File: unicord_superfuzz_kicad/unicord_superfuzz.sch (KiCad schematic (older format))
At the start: 60 parts

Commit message: Add values for most circuit elements
Have not yet added anything for transistors, switch, power supply.
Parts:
- C? (x12): value C -> 10uF
- C?: value C -> 0.002
- C? (x2): value C -> 0.1uF
- C?: value C -> 0.001uF
- R? (x7): value R_US -> 10k
- R? (x3): value R_US -> 470k
- R? (x2): value R_US -> 1.8k
- R? (x3): value R_US -> 47k
- R? (x6): value R_US -> 100k
- R? (x4): value R_US -> 22k
- R?: value R_US -> 150k
- R?: value R_US -> 220k
- R?: value R_US -> 3.3k
- R?: value R_US -> 15k
- R?: value R_US -> 1k
- RV?: value R_POT_US -> 10k
- RV? (x2): value R_POT_US -> 50k
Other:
- moved on the sheet: C?, D?, J?, Q?, R?, RV?, SW?

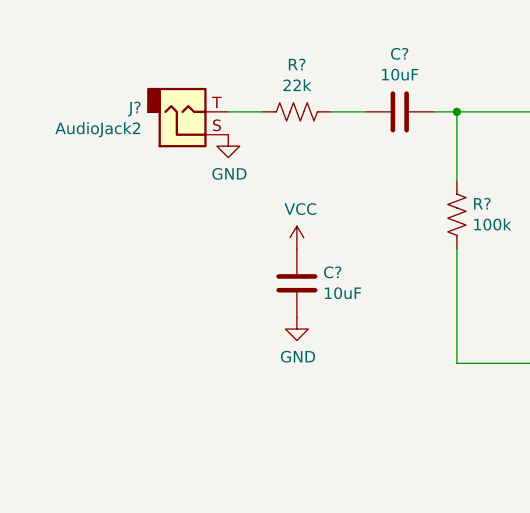
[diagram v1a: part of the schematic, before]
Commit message: Add power/ground to circuit
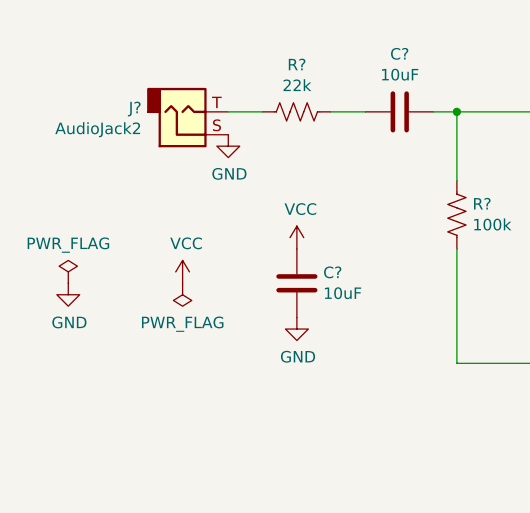
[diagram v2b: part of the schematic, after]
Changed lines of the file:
@@
 	0    1    1    0
 $EndComp
+$Comp
+L power:PWR_FLAG #FLG?
+U 1 1 5ECEB2A7
+P 5000 5950
+F 0 "#FLG?" H 5000 6025 50  0001 C CNN
+F 1 "PWR_FLAG" H 5000 6123 50  0000 C CNN
+F 2 "" H 5000 5950 50  0001 C CNN
+F 3 "~" H 5000 5950 50  0001 C CNN
+	1    5000 5950
+	1    0    0    1
+$EndComp
+$Comp
+L power:VCC #PWR?
+U 1 1 5ED00095
+P 5000 5950
+F 0 "#PWR?" H 5000 5800 50  0001 C CNN
+F 1 "VCC" H 5017 6123 50  0000 C CNN
+F 2 "" H 5000 5950 50  0001 C CNN
+F 3 "" H 5000 5950 50  0001 C CNN
+	1    5000 5950
+	1    0    0    -1
+$EndComp
+$Comp
+L power:PWR_FLAG #FLG?
+U 1 1 5ED3CD5C
+P 4500 5950
+F 0 "#FLG?" H 4500 6025 50  0001 C CNN
+F 1 "PWR_FLAG" H 4500 6123 50  0000 C CNN
+F 2 "" H 4500 5950 50  0001 C CNN
+F 3 "~" H 4500 5950 50  0001 C CNN
+	1    4500 5950
+	1    0    0    -1
+$EndComp
+$Comp
+L power:GND #PWR?
+U 1 1 5ED44778
+P 4500 5950
+F 0 "#PWR?" H 4500 5700 50  0001 C CNN
+F 1 "GND" H 4505 5777 50  0000 C CNN
+F 2 "" H 4500 5950 50  0001 C CNN
+F 3 "" H 4500 5950 50  0001 C CNN
+	1    4500 5950
+	1    0    0    -1
+$EndComp
 $EndSCHEMATC

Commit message: Add annotations to circuit elements
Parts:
- D1, D2: renamed from D?; value D -> DA-90
- gave numbers to parts that had none: 58

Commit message: Add footprints and .net file
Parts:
- C1, C10, C11, C12, C15, C16, C2, C5, C6, C7, C8, C9: footprint (none) -> Capacitor_THT:C_Radial_D5.0mm_H11.0mm_P2.00mm
- C13, C14, C3, C4: footprint (none) -> Capacitor_THT:C_Disc_D5.0mm_W2.5mm_P5.00mm
- D1, D2: footprint (none) -> Diode_THT:D_A-405_P12.70mm_Horizontal
- J1, J2: footprint (none) -> Connector_PinHeader_2.54mm:PinHeader_1x02_P2.54mm_Vertical
- Q1, Q2, Q3, Q4, Q5, Q6: footprint (none) -> Package_TO_SOT_THT:TO-92
- R1, R10, R11, R12, R13, R14, R15, R16, R17, R18, R19, R2, R20, R21, R22, R23, R24, R25, R26, R27, R28, R29, R3, R30, R4, R5, R6, R7, R8, R9: footprint (none) -> Resistor_THT:R_Axial_DIN0204_L3.6mm_D1.6mm_P7.62mm_Horizontal
- RV1, RV3, SW1: footprint (none) -> Connector_PinHeader_2.54mm:PinHeader_1x03_P2.54mm_Vertical
- RV2: footprint (none) -> Potentiometer_THT:Potentiometer_Vishay_43_Horizontal

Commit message: Simulation models added
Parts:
- removed C13: 0.001uF, Capacitor_THT:C_Disc_D5.0mm_W2.5mm_P5.00mm, symbol Device:C
- removed C14: 0.1uF, Capacitor_THT:C_Disc_D5.0mm_W2.5mm_P5.00mm, symbol Device:C
- removed J1, J2: AudioJack2, Connector_PinHeader_2.54mm:PinHeader_1x02_P2.54mm_Vertical, symbol Connector:AudioJack2
- removed RV1, RV3: 50k, Connector_PinHeader_2.54mm:PinHeader_1x03_P2.54mm_Vertical, symbol Device:R_POT_US
- removed RV2: 10k, Potentiometer_THT:Potentiometer_Vishay_43_Horizontal, symbol Device:R_POT_US
- removed SW1: SW_SPDT, Connector_PinHeader_2.54mm:PinHeader_1x03_P2.54mm_Vertical, symbol Switch:SW_SPDT
- added J1, J2, J3: Conn_01x01_Female, symbol Connector:Conn_01x01_Female
- added R31, R32: 22k, Resistor_THT:R_Axial_DIN0204_L3.6mm_D1.6mm_P7.62mm_Horizontal, symbol Device:R_US
- added R33, R34: 3.3k, Resistor_THT:R_Axial_DIN0204_L3.6mm_D1.6mm_P7.62mm_Horizontal, symbol Device:R_US
- C2: Spice_Model (none) -> 10u; Spice_Netlist_Enabled (none) -> Y; Spice_Primitive (none) -> C
- D1, D2: Spice_Lib_File (none) -> 1n34a_for_da-90.lib; Spice_Model (none) -> 1N34A; Spice_Netlist_Enabled (none) -> Y; Spice_Primitive (none) -> D
- Q1, Q4, Q5, Q6: Spice_Lib_File (none) -> BC549_for_2SC539.lib; Spice_Model Q_NPN_ECB -> BC549/550
- Q2, Q3: Spice_Lib_File (none) -> 2N5088_for_2SC828.LIB; Spice_Model Q_NPN_ECB -> 2N5088
- R1, R20, R24: Spice_Model (none) -> 22k; Spice_Netlist_Enabled (none) -> Y; Spice_Primitive (none) -> R
- R25: value 10k -> 22k; Spice_Model (none) -> 22k; Spice_Netlist_Enabled (none) -> Y; Spice_Primitive (none) -> R
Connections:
- net GND: now also R25.2, J2.1 (Pin_1), R33.2, R34.1
- net VCC: now also J3.1 (Pin_1)
- net Input: now reaches R1.2
- net Input: now also J1.1 (Pin_1)
- net at R17.2: now also R33.1
- net at R20.2: now also R34.2
- net at C6.1: now also R31.1
- net at C7.2: now also R31.2, R32.1
- net at R9.1: now also R32.2
- net at C12.1, R22.1: no longer R24.1
- net at R22.2, R23.1: now also R24.1
- net at R24.2: now also C15.2, R25.1; no longer R25.2
- net Output: now reaches C16.1, R30.1
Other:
- moved on the sheet: R9
